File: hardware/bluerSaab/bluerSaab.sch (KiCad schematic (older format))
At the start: 6 parts, among them J1 Conn_01x12, U1 LM2596, U2 PCM5102, U3 ESP32-DEVKITC, U4 MCP2515

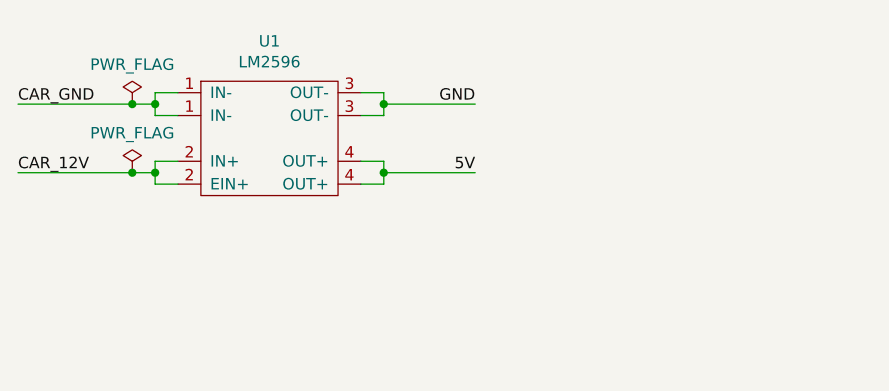
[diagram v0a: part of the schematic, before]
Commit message: Fuse added
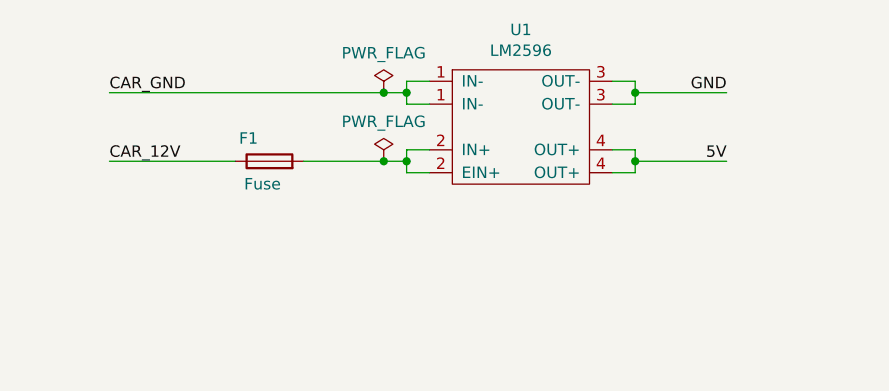
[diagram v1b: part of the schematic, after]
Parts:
- added F1: Fuse, symbol Device:Fuse
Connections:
- net CAR_12V: now also F1.1; no longer U1.2 (IN+)
- new net: F1.2, U1.2 (IN+)
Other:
- moved on the sheet: U1
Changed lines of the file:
@@
 L bluerSaab:LM2596 U1
 U 1 1 5D068B16
-P 2050 1300
-F 0 "U1" H 2050 1725 50  0000 C CNN
-F 1 "LM2596" H 2050 1634 50  0000 C CNN
-F 2 "" H 2050 1600 50  0001 C CNN
-F 3 "" H 2050 1600 50  0001 C CNN
-	1    2050 1300
+P 3150 1250
+F 0 "U1" H 3150 1675 50  0000 C CNN
+F 1 "LM2596" H 3150 1584 50  0000 C CNN
+F 2 "" H 3150 1550 50  0001 C CNN
+F 3 "" H 3150 1550 50  0001 C CNN
+	1    3150 1250
 	1    0    0    -1
 $EndComp
@@
 $EndComp
 Wire Wire Line
-	1650 1200 1550 1200
-Wire Wire Line
-	1550 1200 1550 1150
-Wire Wire Line
-	1550 1100 1650 1100
-Wire Wire Line
-	1650 1400 1550 1400
-Wire Wire Line
-	1550 1400 1550 1450
-Wire Wire Line
-	1550 1500 1650 1500
-Wire Wire Line
-	2450 1500 2550 1500
-Wire Wire Line
-	2550 1500 2550 1450
-Wire Wire Line
-	2550 1400 2450 1400
-Wire Wire Line
-	2450 1200 2550 1200
-Wire Wire Line
-	2550 1200 2550 1150
-Wire Wire Line
-	2550 1100 2450 1100
-Wire Wire Line
-	1550 1150 1450 1150
-Connection ~ 1550 1150
-Wire Wire Line
-	1550 1150 1550 1100
-Wire Wire Line
-	1550 1450 1450 1450
-Connection ~ 1550 1450
-Wire Wire Line
-	1550 1450 1550 1500
-Text Label 950  1150 0    50   ~ 0
+	2750 1150 2650 1150
+Wire Wire Line
+	2650 1150 2650 1100
+Wire Wire Line
+	2650 1050 2750 1050
+Wire Wire Line
+	2750 1350 2650 1350
+Wire Wire Line
+	2650 1350 2650 1400
+Wire Wire Line
+	2650 1450 2750 1450
+Wire Wire Line
+	3550 1450 3650 1450
+Wire Wire Line
+	3650 1450 3650 1400
+Wire Wire Line
+	3650 1350 3550 1350
+Wire Wire Line
+	3550 1150 3650 1150
+Wire Wire Line
+	3650 1150 3650 1100
+Wire Wire Line
+	3650 1050 3550 1050
+Wire Wire Line
+	2650 1100 2550 1100
+Connection ~ 2650 1100
+Wire Wire Line
+	2650 1100 2650 1050
+Wire Wire Line
+	2650 1400 2550 1400
+Connection ~ 2650 1400
+Wire Wire Line
+	2650 1400 2650 1450
+Text Label 1350 1100 0    50   ~ 0
 CAR_GND
-Text Label 950  1450 0    50   ~ 0
+Text Label 1350 1400 0    50   ~ 0
 CAR_12V
-Text Label 2950 1150 2    50   ~ 0
-GND
-Text Label 2950 1450 2    50   ~ 0
+Text Label 4050 1100 2    50   ~ 0
+GND
+Text Label 4050 1400 2    50   ~ 0
 5V
-Connection ~ 2550 1450
-Wire Wire Line
-	2550 1450 2550 1400
-Connection ~ 2550 1150
-Wire Wire Line
-	2550 1150 2550 1100
+Connection ~ 3650 1400
+Wire Wire Line
+	3650 1400 3650 1350
+Connection ~ 3650 1100
+Wire Wire Line
+	3650 1100 3650 1050
 $Comp
 L power:PWR_FLAG #FLG01
 U 1 1 5D06E557
-P 1450 1150
-F 0 "#FLG01" H 1450 1225 50  0001 C CNN
-F 1 "PWR_FLAG" H 1450 1323 50  0000 C CNN
-F 2 "" H 1450 1150 50  0001 C CNN
-F 3 "~" H 1450 1150 50  0001 C CNN
-	1    1450 1150
-	1    0    0    -1
-$EndComp
-Connection ~ 1450 1150
-Wire Wire Line
-	1450 1150 950  1150
+P 2550 1100
+F 0 "#FLG01" H 2550 1175 50  0001 C CNN
+F 1 "PWR_FLAG" H 2550 1273 50  0000 C CNN
+F 2 "" H 2550 1100 50  0001 C CNN
+F 3 "~" H 2550 1100 50  0001 C CNN
+	1    2550 1100
+	1    0    0    -1
+$EndComp
+Connection ~ 2550 1100
+Wire Wire Line
+	2550 1100 1350 1100
 $Comp
 L power:PWR_FLAG #FLG03
 U 1 1 5D06EF9A
-P 1450 1450
-F 0 "#FLG03" H 1450 1525 50  0001 C CNN
-F 1 "PWR_FLAG" H 1450 1623 50  0000 C CNN
-F 2 "" H 1450 1450 50  0001 C CNN
-F 3 "~" H 1450 1450 50  0001 C CNN
-	1    1450 1450
-	1    0    0    -1
-$EndComp
-Connection ~ 1450 1450
-Wire Wire Line
-	1450 1450 950  1450
+P 2550 1400
+F 0 "#FLG03" H 2550 1475 50  0001 C CNN
+F 1 "PWR_FLAG" H 2550 1573 50  0000 C CNN
+F 2 "" H 2550 1400 50  0001 C CNN
+F 3 "~" H 2550 1400 50  0001 C CNN
+	1    2550 1400
+	1    0    0    -1
+$EndComp
 Text Label 5350 2550 0    50   ~ 0
 5V
@@
 	9600 4300 8900 4300
 Wire Wire Line
-	2550 1150 2950 1150
-Wire Wire Line
-	2550 1450 2950 1450
+	3650 1100 4050 1100
+Wire Wire Line
+	3650 1400 4050 1400
 $Comp
 L Jumper:SolderJumper_2_Open JP1
@@
 Wire Wire Line
 	5200 2650 5100 2650
+$Comp
+L Device:Fuse F1
+U 1 1 5D0E6F79
+P 2050 1400
+F 0 "F1" V 2150 1450 50  0000 L CNN
+F 1 "Fuse" V 1950 1350 50  0000 L CNN
+F 2 "" V 1980 1400 50  0001 C CNN
+F 3 "~" H 2050 1400 50  0001 C CNN
+	1    2050 1400
+	0    -1   -1   0
+$EndComp
+Wire Wire Line
+	2550 1400 2200 1400
+Connection ~ 2550 1400
+Wire Wire Line
+	1900 1400 1350 1400
 $EndSCHEMATC

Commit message: Initial layout -missing footprints for conn and fuse
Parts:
- JP1: footprint (none) -> Jumper:SolderJumper-2_P1.3mm_Open_TrianglePad1.0x1.5mm
- U1: footprint (none) -> bluerSaab:LM2596
- U2: footprint (none) -> bluerSaab:PCM5102
- U3: footprint (none) -> bluerSaab:ESP32-DEVKITC
- U4: footprint (none) -> bluerSaab:MCP2515
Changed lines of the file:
@@
 EESchema Schematic File Version 4
+LIBS:bluerSaab-cache
 EELAYER 29 0
 EELAYER END
@@
 F 0 "U3" H 2750 4575 50  0000 C CNN
 F 1 "ESP32-DEVKITC" H 2750 4484 50  0000 C CNN
-F 2 "" H 2750 4450 50  0001 C CNN
+F 2 "bluerSaab:ESP32-DEVKITC" H 2750 4450 50  0001 C CNN
 F 3 "" H 2750 4450 50  0001 C CNN
 	1    2750 3550
@@
 F 0 "U1" H 3150 1675 50  0000 C CNN
 F 1 "LM2596" H 3150 1584 50  0000 C CNN
-F 2 "" H 3150 1550 50  0001 C CNN
+F 2 "bluerSaab:LM2596" H 3150 1550 50  0001 C CNN
 F 3 "" H 3150 1550 50  0001 C CNN
 	1    3150 1250
@@
 F 0 "U4" H 6250 5225 50  0000 C CNN
 F 1 "MCP2515" H 6250 5134 50  0000 C CNN
-F 2 "" H 6250 5150 50  0001 C CNN
+F 2 "bluerSaab:MCP2515" H 6250 5150 50  0001 C CNN
 F 3 "" H 6250 5150 50  0001 C CNN
 	1    6250 4700
@@
 F 0 "U2" H 6250 3775 50  0000 C CNN
 F 1 "PCM5102" H 6250 3684 50  0000 C CNN
-F 2 "" H 6250 3650 50  0001 C CNN
+F 2 "bluerSaab:PCM5102" H 6250 3650 50  0001 C CNN
 F 3 "" H 6250 3650 50  0001 C CNN
 	1    6250 3050
@@
 F 0 "JP1" V 5050 2850 50  0000 L CNN
 F 1 "SolderJumper_2_Open" V 5150 2200 50  0000 L CNN
-F 2 "" H 5100 3050 50  0001 C CNN
+F 2 "Jumper:SolderJumper-2_P1.3mm_Open_TrianglePad1.0x1.5mm" H 5100 3050 50  0001 C CNN
 F 3 "~" H 5100 3050 50  0001 C CNN
 	1    5100 3050

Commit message: some tracing done
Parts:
- F1: footprint (none) -> Fuse:Fuseholder_Cylinder-5x20mm_Stelvio-Kontek_PTF78_Horizontal_Open
- J1: footprint (none) -> bluerSaab:SAAB_CDC
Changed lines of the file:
@@
 F 0 "J1" H 9880 3692 50  0000 L CNN
 F 1 "Conn_01x12" H 9880 3601 50  0000 L CNN
-F 2 "" H 9800 3700 50  0001 C CNN
+F 2 "bluerSaab:SAAB_CDC" H 9800 3700 50  0001 C CNN
 F 3 "~" H 9800 3700 50  0001 C CNN
 	1    9800 3700
@@
 F 0 "F1" V 2150 1450 50  0000 L CNN
 F 1 "Fuse" V 1950 1350 50  0000 L CNN
-F 2 "" V 1980 1400 50  0001 C CNN
+F 2 "Fuse:Fuseholder_Cylinder-5x20mm_Stelvio-Kontek_PTF78_Horizontal_Open" V 1980 1400 50  0001 C CNN
 F 3 "~" H 2050 1400 50  0001 C CNN
 	1    2050 1400

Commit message: PCB minified to bring the size below 10x10cm
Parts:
- F1: footprint Fuse:Fuseholder_Cylinder-5x20mm_Stelvio-Kontek_PTF78_Horizontal_Open -> Fuse_Holders_and_Fuses:Fuseholder_Fuse_TR5_Littlefuse-No560_No460
- U1: symbol bluerSaab:LM2596 -> bluerSaab-rescue:LM2596-bluerSaab
- U2: symbol bluerSaab:PCM5102 -> bluerSaab-rescue:PCM5102-bluerSaab
- U3: symbol bluerSaab:ESP32-DEVKITC -> bluerSaab-rescue:ESP32-DEVKITC-bluerSaab
- U4: symbol bluerSaab:MCP2515 -> bluerSaab-rescue:MCP2515-bluerSaab
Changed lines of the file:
@@
 $EndDescr
 $Comp
-L bluerSaab:ESP32-DEVKITC U3
+L bluerSaab-rescue:ESP32-DEVKITC-bluerSaab U3
 U 1 1 5D068673
 P 2750 3550
@@
 $EndComp
 $Comp
-L bluerSaab:LM2596 U1
+L bluerSaab-rescue:LM2596-bluerSaab U1
 U 1 1 5D068B16
 P 3150 1250
@@
 $EndComp
 $Comp
-L bluerSaab:MCP2515 U4
+L bluerSaab-rescue:MCP2515-bluerSaab U4
 U 1 1 5D068DEA
 P 6250 4700
@@
 $EndComp
 $Comp
-L bluerSaab:PCM5102 U2
+L bluerSaab-rescue:PCM5102-bluerSaab U2
 U 1 1 5D069228
 P 6250 3050
@@
 F 0 "F1" V 2150 1450 50  0000 L CNN
 F 1 "Fuse" V 1950 1350 50  0000 L CNN
-F 2 "Fuse:Fuseholder_Cylinder-5x20mm_Stelvio-Kontek_PTF78_Horizontal_Open" V 1980 1400 50  0001 C CNN
+F 2 "Fuse_Holders_and_Fuses:Fuseholder_Fuse_TR5_Littlefuse-No560_No460" V 1980 1400 50  0001 C CNN
 F 3 "~" H 2050 1400 50  0001 C CNN
 	1    2050 1400
